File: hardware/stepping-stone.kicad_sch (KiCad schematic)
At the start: 0 parts

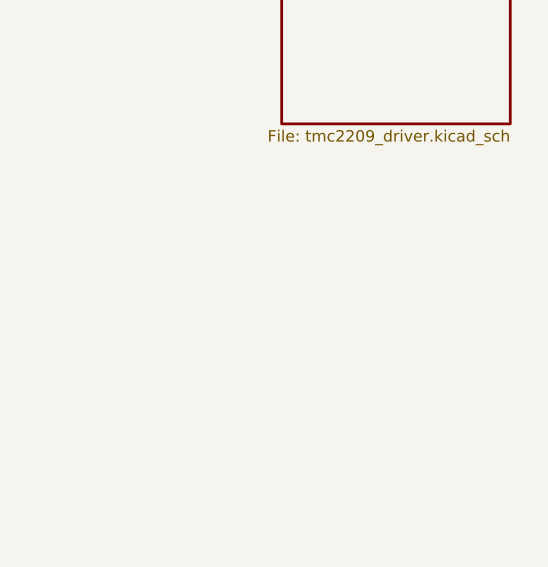
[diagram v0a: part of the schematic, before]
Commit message: Begin SD card implementation
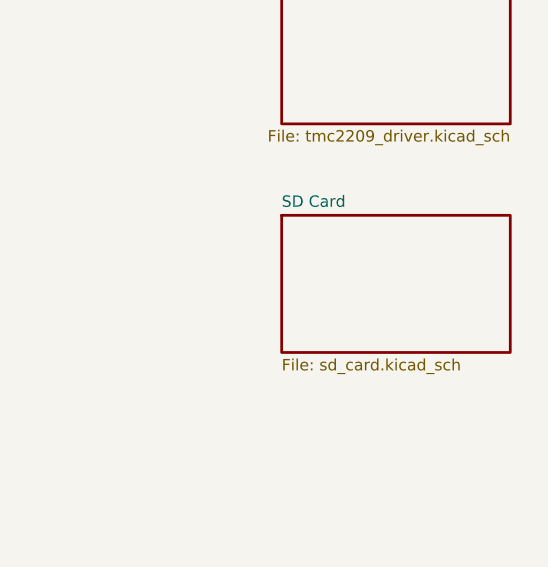
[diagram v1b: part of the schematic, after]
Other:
- added sheet SD Card (sd_card.kicad_sch)
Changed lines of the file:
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@@
+	)
+	(sheet
+		(at 190.5 76.2)
+		(size 25.4 15.24)
+		(exclude_from_sim no)
+		(in_bom yes)
+		(on_board yes)
+		(dnp no)
+		(fields_autoplaced yes)
+		(stroke
+			(width 0.3048)
+			(type solid)
+		)
+		(fill
+			(color 255 229 191 1)
+		)
+		(property "Sheetname" "SD Card"
+			(at 190.5 75.4122 0)
+			(show_name no)
+			(do_not_autoplace no)
+			(effects
+				(font
+					(size 1.27 1.27)
+				)
+				(justify left bottom)
+			)
+		)
+		(property "Sheetfile" "sd_card.kicad_sch"
+			(at 190.5 92.1008 0)
+			(show_name no)
+			(do_not_autoplace no)
+			(effects
+				(font
+					(size 1.27 1.27)
+				)
+				(justify left top)
+			)
+		)
+		(instances
+			(project "stepping-stone"
+				(path "/793a882e-3f7b-468b-a863-41a1f527e1bf"
+					(page "8")
+				)
+			)
+		)
 	)
 	(sheet

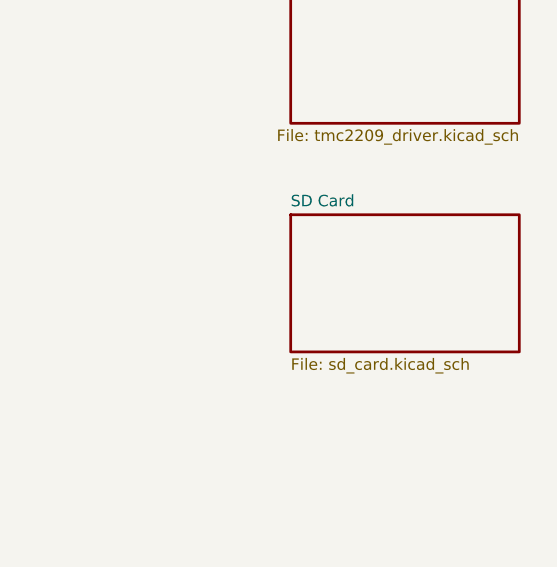
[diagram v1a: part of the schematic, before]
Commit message: ESTOP control refinement
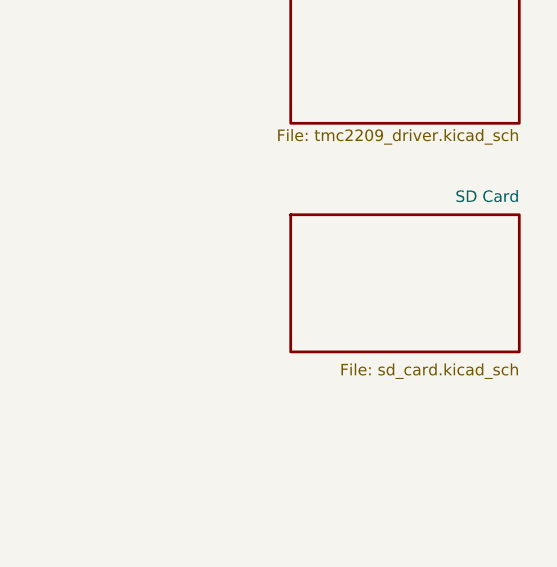
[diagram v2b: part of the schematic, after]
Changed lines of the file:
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@@
 		(on_board yes)
 		(dnp no)
-		(fields_autoplaced yes)
 		(stroke
 			(width 0.3048)
@@
 		)
 		(property "Sheetname" "SD Card"
-			(at 190.5 75.4122 0)
+			(at 215.9 74.93 0)
 			(show_name no)
 			(do_not_autoplace no)
@@
 					(size 1.27 1.27)
 				)
-				(justify left bottom)
+				(justify right bottom)
 			)
 		)
 		(property "Sheetfile" "sd_card.kicad_sch"
-			(at 190.5 92.1008 0)
+			(at 215.9 92.71 0)
 			(show_name no)
 			(do_not_autoplace no)
@@
 					(size 1.27 1.27)
 				)
-				(justify left top)
+				(justify right top)
 			)
 		)
